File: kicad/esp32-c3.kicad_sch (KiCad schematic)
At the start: 18 parts, among them U3 SN65HVD230, U5 ESP32-C3-MINI-1

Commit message: BOM updates with a few more alternative parts
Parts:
- U3: Manufacturer (none) -> Texas Instruments; PartNumber (none) -> SN65HVD230D; Remarks (none) -> Alternative: SN65HVD230QDR
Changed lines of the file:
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@@
+      (effects (font (size 1.27 1.27)) hide)
+    )
+    (property "Manufacturer" "Texas Instruments" (id 7) (at 205.74 71.12 0)
+      (effects (font (size 1.27 1.27)) hide)
+    )
+    (property "PartNumber" "SN65HVD230D" (id 8) (at 205.74 71.12 0)
+      (effects (font (size 1.27 1.27)) hide)
+    )
+    (property "Remarks" "Alternative: SN65HVD230QDR" (id 9) (at 205.74 71.12 0)
       (effects (font (size 1.27 1.27)) hide)
     )

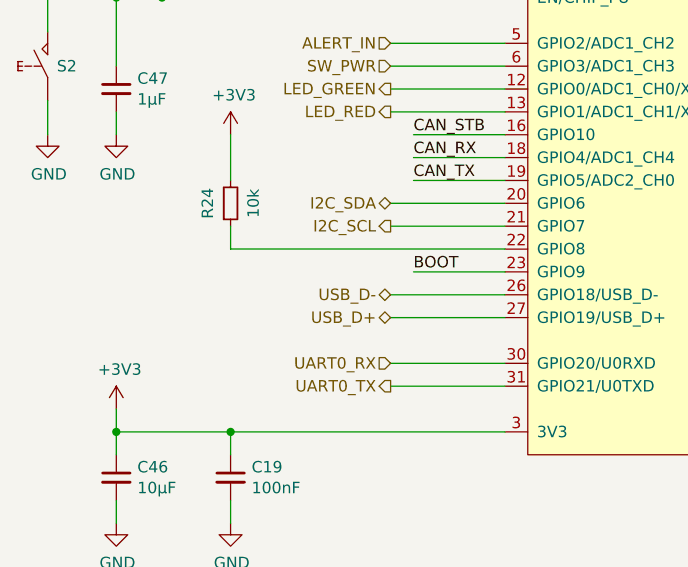
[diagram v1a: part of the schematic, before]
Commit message: Board v0.3.1: Add test point for GPIO9 (BOOT) pin
Fixes #34
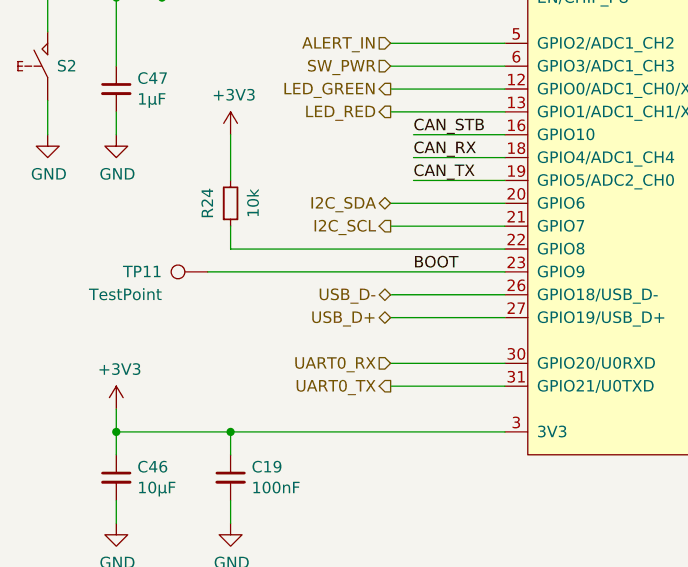
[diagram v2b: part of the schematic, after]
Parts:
- added TP11: TestPoint, TestPoint:TestPoint_Pad_D1.5mm, symbol Connector:TestPoint
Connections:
- net BOOT: now also TP11.1
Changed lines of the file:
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@@
   (title_block
     (title "Libre Solar BMS C1")
-    (date "2022-08-27")
-    (rev "0.3")
+    (date "2022-09-30")
+    (rev "0.3.1")
     (company "Libre Solar Technologies GmbH")
     (comment 1 "Website: https://libre.solar")
@@
     (stroke (width 0) (type solid) (color 0 0 0 0))
   )
-  (wire (pts (xy 81.28 88.9) (xy 91.44 88.9))
+  (wire (pts (xy 58.42 88.9) (xy 91.44 88.9))
     (stroke (width 0) (type default) (color 0 0 0 0))
   )
@@
     (pin "2")
   )
+  (symbol (lib_id "Connector:TestPoint") (at 58.42 88.9 90) (unit 1)
+    (in_bom yes) (on_board yes)
+    (property "Reference" "TP11" (id 0) (at 53.34 88.9 90)
+      (effects (font (size 1.27 1.27)) (justify left))
+    )
+    (property "Value" "TestPoint" (id 1) (at 53.34 91.44 90)
+      (effects (font (size 1.27 1.27)) (justify left))
+    )
+    (property "Footprint" "TestPoint:TestPoint_Pad_D1.5mm" (id 2) (at 58.42 88.9 0)
+      (effects (font (size 1.27 1.27)) hide)
+    )
+    (property "Datasheet" "" (id 3) (at 58.42 88.9 0)
+      (effects (font (size 1.27 1.27)) hide)
+    )
+    (pin "1")
+  )
   (symbol (lib_id "LibreSolar:C") (at 238.76 81.28 90) (unit 1)

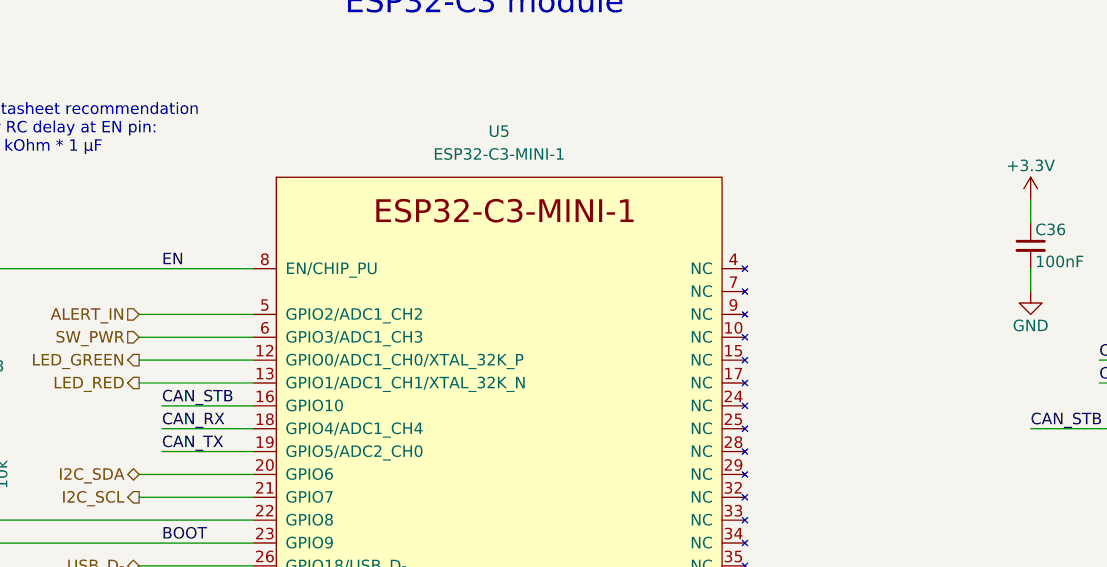
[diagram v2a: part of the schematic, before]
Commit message: Add ESP32-C3 and switch part numbers
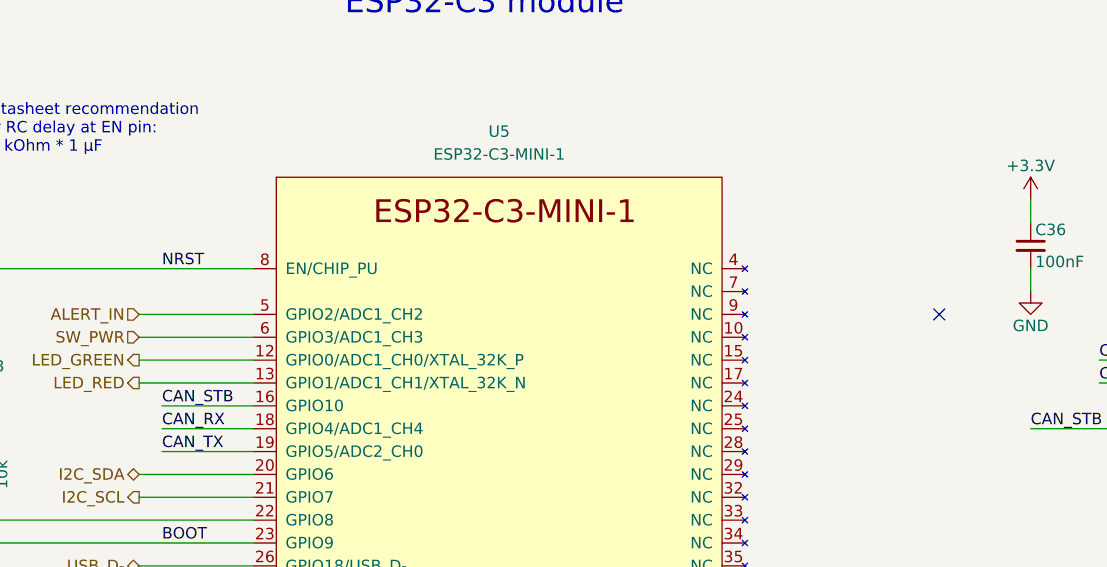
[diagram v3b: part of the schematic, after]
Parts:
- S2: Manufacturer (none) -> E-Switch; PartNumber (none) -> TL3305AF160QG
- U5: Manufacturer (none) -> Espressif Systems
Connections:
- net EN renamed NRST
- no-connect marks 1 -> 2
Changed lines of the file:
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@@
   )
   (no_connect (at 195.58 73.66))
+  (no_connect (at 167.64 63.5))
   (wire (pts (xy 48.26 58.42) (xy 53.34 58.42))
     (stroke (width 0) (type default) (color 0 0 0 0))
@@
     (effects (font (size 1.27 1.27)) (justify left bottom))
   )
-  (label "EN" (at 81.28 58.42 0)
+  (label "NRST" (at 81.28 58.42 0)
     (effects (font (size 1.27 1.27)) (justify left bottom))
   )
@@
     )
     (property "PartNumber" "ESP32-C3-MINI-1-N4" (id 4) (at 118.11 80.01 0)
+      (effects (font (size 1.27 1.27)) hide)
+    )
+    (property "Manufacturer" "Espressif Systems" (id 5) (at 118.11 80.01 0)
       (effects (font (size 1.27 1.27)) hide)
     )
@@
     )
     (property "Datasheet" "" (id 3) (at 40.64 66.04 0))
-    (pin "1")
-    (pin "2")
+    (property "Manufacturer" "E-Switch" (id 4) (at 40.64 66.04 0)
+      (effects (font (size 1.27 1.27)) hide)
+    )
+    (property "PartNumber" "TL3305AF160QG" (id 5) (at 40.64 66.04 0)
+      (effects (font (size 1.27 1.27)) hide)
+    )
+    (pin "1")
+    (pin "2")

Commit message: v3.2.2: Switch to SMD terminals instead of press-fit
Rationale: These are easier to manufacture (no additional step required)
and the PCB can be mounted onto a heat sink without any milling required.
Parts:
- C19, C46, C47, R24, R68: Config +esp32 -> (none)
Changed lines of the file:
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@@
   (title_block
     (title "Libre Solar BMS C1")
-    (date "2022-09-30")
-    (rev "0.3.1")
+    (date "2022-11-07")
+    (rev "0.3.2")
     (company "Libre Solar Technologies GmbH")
     (comment 1 "Website: https://libre.solar")
@@
       (effects (font (size 1.27 1.27)) hide)
     )
-    (property "Config" "+esp32" (id 7) (at 48.26 111.76 0)
+    (property "Config" "" (id 7) (at 48.26 111.76 0)
       (effects (font (size 1.27 1.27)) hide)
     )
@@
       (effects (font (size 1.27 1.27)) hide)
     )
-    (property "Config" "+esp32" (id 5) (at 48.26 68.58 0)
+    (property "Config" "" (id 5) (at 48.26 68.58 0)
       (effects (font (size 1.27 1.27)) hide)
     )
     (property "Manufacturer" "any" (id 6) (at 48.26 68.58 0)
-      (effects (font (size 1.27 1.27)) hide)
-    )
-    (property "Remarks" "" (id 7) (at 48.26 68.58 0)
       (effects (font (size 1.27 1.27)) hide)
     )
@@
       (effects (font (size 1.27 1.27)) hide)
     )
-    (property "Config" "+esp32" (id 6) (at 53.34 50.8 0)
+    (property "Config" "" (id 6) (at 53.34 50.8 0)
       (effects (font (size 1.27 1.27)) hide)
     )
@@
       (effects (font (size 1.27 1.27)) hide)
     )
-    (property "Config" "+esp32" (id 6) (at 60.96 81.28 0)
+    (property "Config" "" (id 6) (at 60.96 81.28 0)
       (effects (font (size 1.27 1.27)) hide)
     )
@@
       (effects (font (size 1.27 1.27)) hide)
     )
-    (property "Config" "+esp32" (id 5) (at 60.96 111.76 0)
-      (effects (font (size 1.27 1.27)) hide)
-    )
+    (property "Config" "" (id 5) (at 60.96 111.76 0)
+      (effects (font (size 1.27 1.27)) hide)
+    )

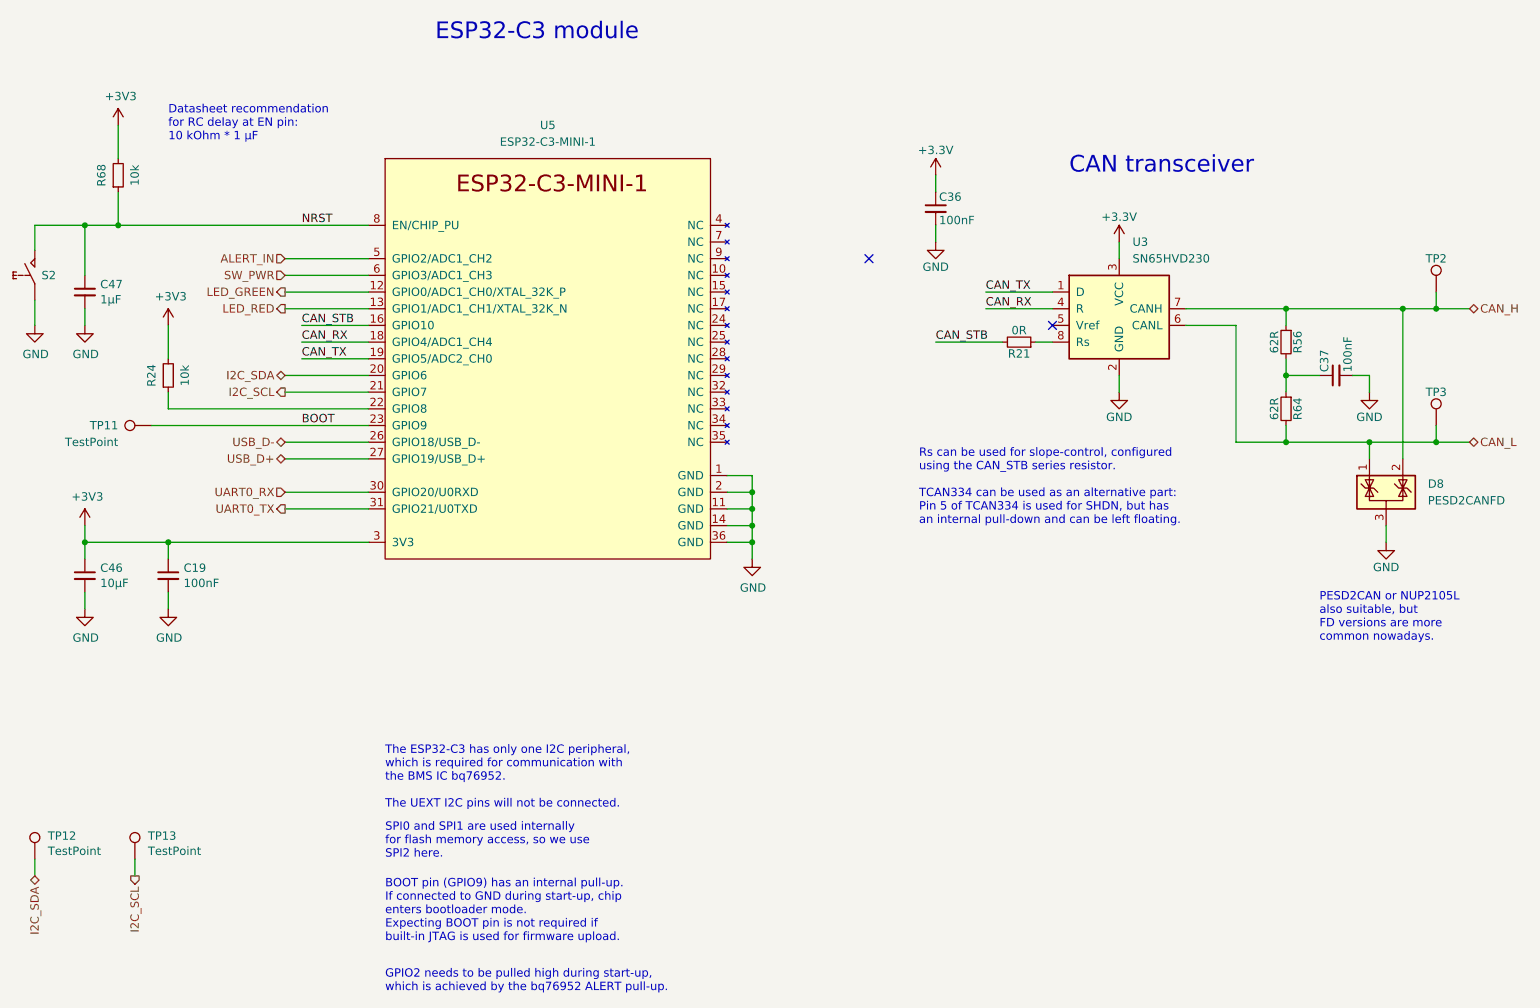
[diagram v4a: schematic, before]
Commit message: v0.3.3: Final version for BMS challenge with EnAccess
Updates compared to v0.3.2:

- Optimization of some copper planes
- Net tie with thicker connection to GND
- D12 connected to Bat-

No parts were changed, the BOM is same as before.
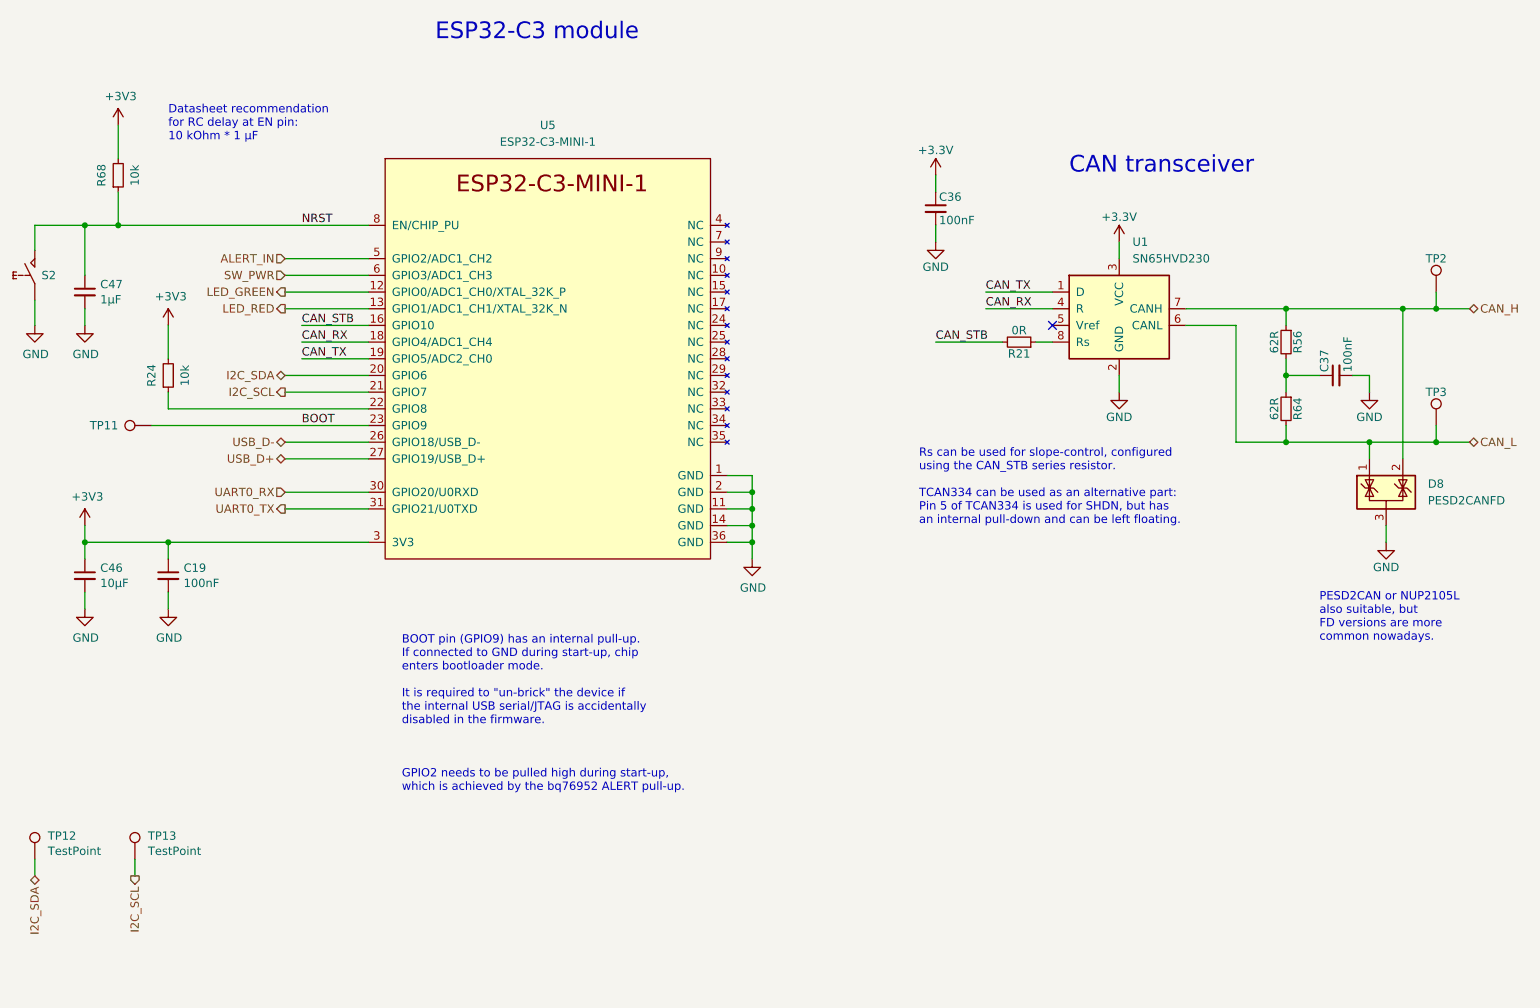
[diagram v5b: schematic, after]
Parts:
- renumbered U3 to U1
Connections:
- no-connect marks 2 -> 1
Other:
- note added: "BOOT pin (GPIO9) has an internal pull-up. If connected to GND during start-up, chip enters bootloader mode. It is required to "un-brick" the device if the internal USB serial/JTAG is accidentally disabled in the firmware."
- note removed: "BOOT pin (GPIO9) has an internal pull-up. If connected to GND during start-up, chip enters bootloader mode. Expecting BOOT pin is not required if built-in JTAG is used for firmware upload."
- note removed: "SPI0 and SPI1 are used internally for flash memory access, so we use SPI2 here."
- note removed: "The ESP32-C3 has only one I2C peripheral, which is required for communication with the BMS IC bq76952. The UEXT I2C pins will not be connected."
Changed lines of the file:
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@@
   (title_block
     (title "Libre Solar BMS C1")
-    (date "2022-11-07")
-    (rev "0.3.2")
+    (date "2022-11-21")
+    (rev "0.3.3")
     (company "Libre Solar Technologies GmbH")
     (comment 1 "Website: https://libre.solar")
@@
   )
   (no_connect (at 195.58 73.66))
-  (no_connect (at 167.64 63.5))
   (wire (pts (xy 48.26 58.42) (xy 53.34 58.42))
     (stroke (width 0) (type default) (color 0 0 0 0))
@@
   )
   (text "GPIO2 needs to be pulled high during start-up,\nwhich is achieved by the bq76952 ALERT pull-up."
-    (at 93.98 175.26 0)
-    (effects (font (size 1.27 1.27)) (justify left bottom))
-  )
-  (text "SPI0 and SPI1 are used internally\nfor flash memory access, so we use\nSPI2 here."
-    (at 93.98 154.94 0)
-    (effects (font (size 1.27 1.27)) (justify left bottom))
-  )
-  (text "BOOT pin (GPIO9) has an internal pull-up.\nIf connected to GND during start-up, chip\nenters bootloader mode.\nExpecting BOOT pin is not required if \nbuilt-in JTAG is used for firmware upload."
-    (at 93.98 167.64 0)
+    (at 96.52 144.78 0)
+    (effects (font (size 1.27 1.27)) (justify left bottom))
+  )
+  (text "BOOT pin (GPIO9) has an internal pull-up.\nIf connected to GND during start-up, chip\nenters bootloader mode.\n\nIt is required to \"un-brick\" the device if\nthe internal USB serial/JTAG is accidentally\ndisabled in the firmware."
+    (at 96.52 134.62 0)
     (effects (font (size 1.27 1.27)) (justify left bottom))
   )
@@
   (text "Rs can be used for slope-control, configured\nusing the CAN_STB series resistor.\n\nTCAN334 can be used as an alternative part:\nPin 5 of TCAN334 is used for SHDN, but has\nan internal pull-down and can be left floating."
     (at 175.26 104.14 0)
-    (effects (font (size 1.27 1.27)) (justify left bottom))
-  )
-  (text "The ESP32-C3 has only one I2C peripheral,\nwhich is required for communication with\nthe BMS IC bq76952.\n\nThe UEXT I2C pins will not be connected."
-    (at 93.98 147.32 0)
     (effects (font (size 1.27 1.27)) (justify left bottom))
   )
@@
     )
     (property "Value" "TestPoint" (id 1) (at 53.34 91.44 90)
-      (effects (font (size 1.27 1.27)) (justify left))
+      (effects (font (size 1.27 1.27)) (justify left) hide)
     )
     (property "Footprint" "TestPoint:TestPoint_Pad_D1.5mm" (id 2) (at 58.42 88.9 0)
@@
       (effects (font (size 1.27 1.27)) hide)
     )
-    (property "Reference" "U3" (id 5) (at 205.74 71.12 0)
-      (effects (font (size 1.27 1.27)) hide)
-    )
-    (property "Value" "SN65HVD230" (id 6) (at 205.74 71.12 0)
-      (effects (font (size 1.27 1.27)) hide)
-    )
